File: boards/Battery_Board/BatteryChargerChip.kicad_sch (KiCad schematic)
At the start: 13 parts, among them J201 Conn_01x02, Q201 BSP613PH6327XTSA1, U201 BQ25185DLHR, U202 TCA6424

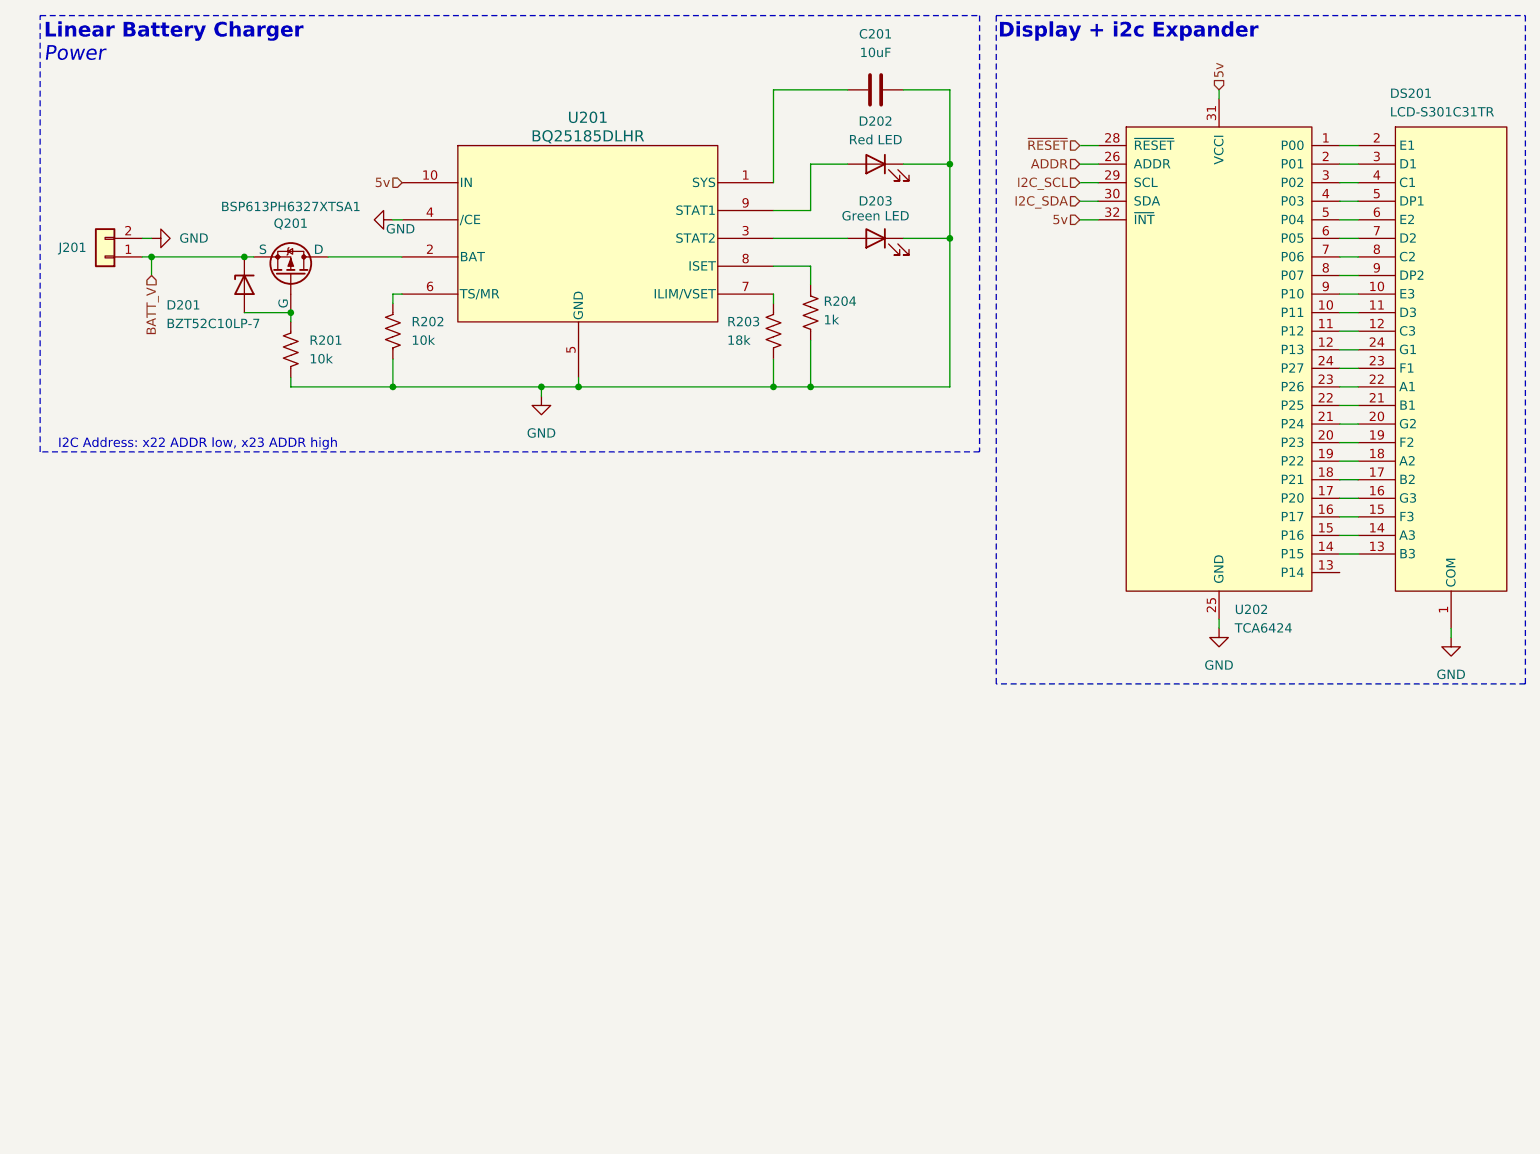
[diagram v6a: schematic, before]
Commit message: routing for displays 1-3
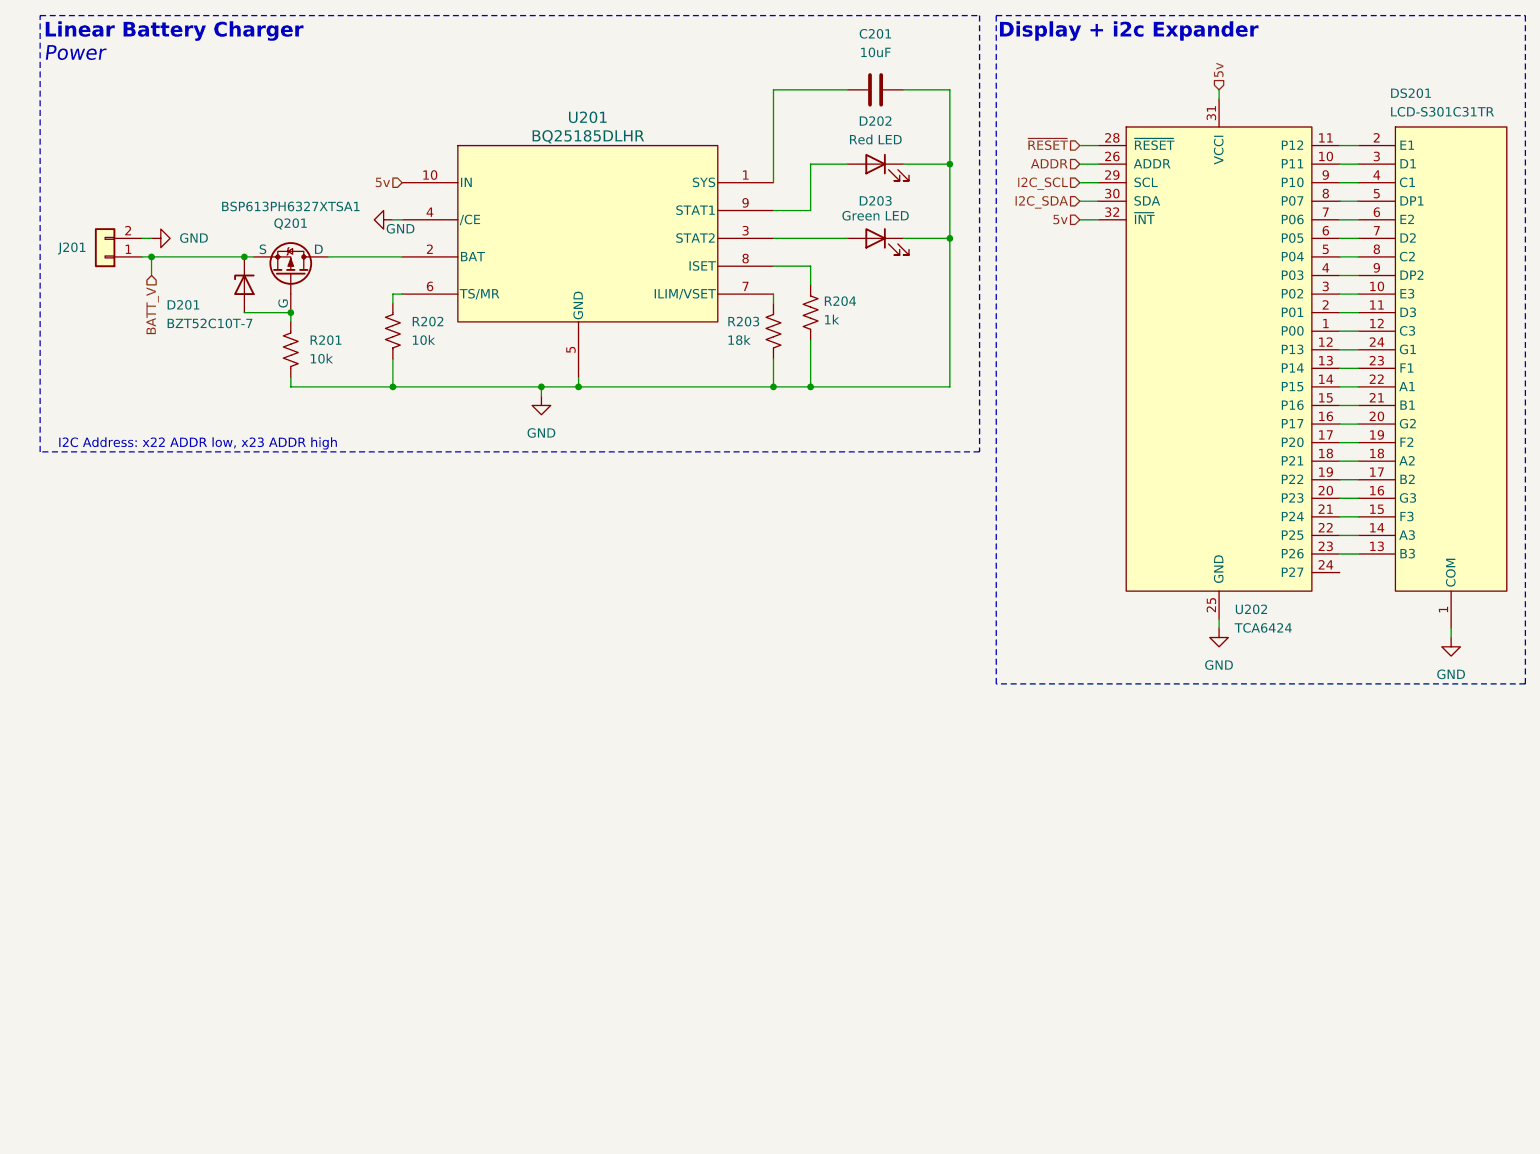
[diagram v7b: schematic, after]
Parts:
- D201: value BZT52C10LP-7 -> BZT52C10T-7; footprint Diode_SMD:D_0402_1005Metric -> Diode_SMD:D_SOD-523
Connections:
- net at DS201.10 (E3): now also U202.3 (P02); no longer U202.9 (P10)
- net at DS201.11 (D3): now also U202.2 (P01); no longer U202.10 (P11)
- net at DS201.12 (C3): now also U202.1 (P00); no longer U202.11 (P12)
- net at DS201.13 (B3): now also U202.23 (P26); no longer U202.14 (P15)
- net at DS201.14 (A3): now also U202.22 (P25); no longer U202.15 (P16)
- net at DS201.15 (F3): now also U202.21 (P24); no longer U202.16 (P17)
- net at DS201.16 (G3): now also U202.20 (P23); no longer U202.17 (P20)
- net at DS201.17 (B2): now also U202.19 (P22); no longer U202.18 (P21)
- net at DS201.18 (A2): now also U202.18 (P21); no longer U202.19 (P22)
- net at DS201.19 (F2): now also U202.17 (P20); no longer U202.20 (P23)
- net at DS201.2 (E1): now also U202.11 (P12); no longer U202.1 (P00)
- net at DS201.20 (G2): now also U202.16 (P17); no longer U202.21 (P24)
- net at DS201.21 (B1): now also U202.15 (P16); no longer U202.22 (P25)
- net at DS201.22 (A1): now also U202.14 (P15); no longer U202.23 (P26)
- net at DS201.23 (F1): now also U202.13 (P14); no longer U202.24 (P27)
- net at DS201.3 (D1): now also U202.10 (P11); no longer U202.2 (P01)
- net at DS201.4 (C1): now also U202.9 (P10); no longer U202.3 (P02)
- net at DS201.5 (DP1): now also U202.8 (P07); no longer U202.4 (P03)
- net at DS201.6 (E2): now also U202.7 (P06); no longer U202.5 (P04)
- net at DS201.8 (C2): now also U202.5 (P04); no longer U202.7 (P06)
- net at DS201.9 (DP2): now also U202.4 (P03); no longer U202.8 (P07)

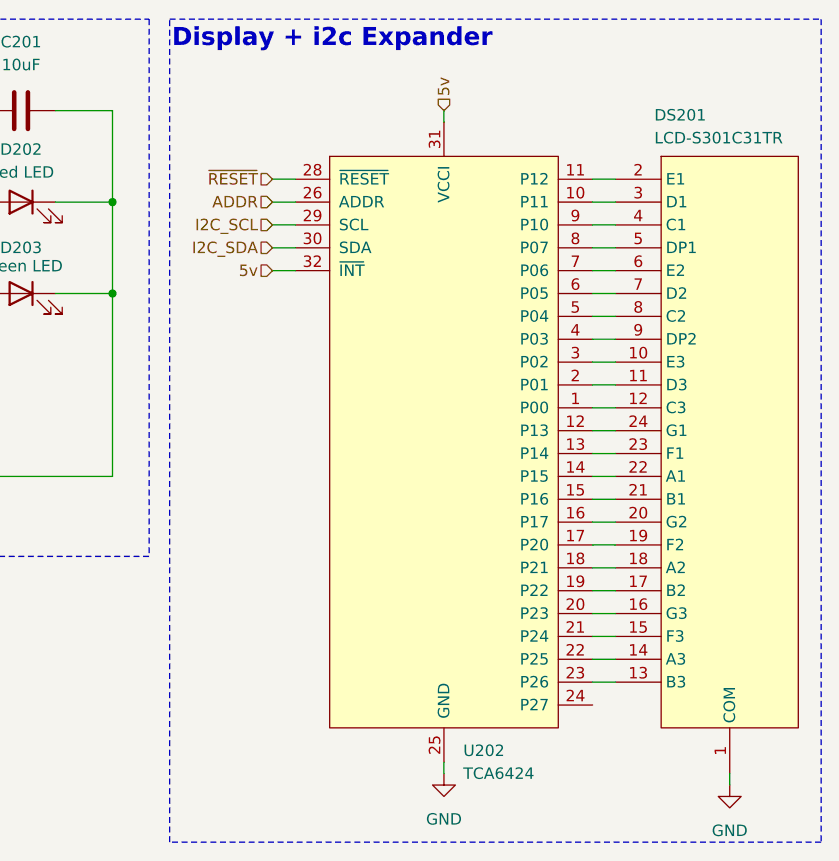
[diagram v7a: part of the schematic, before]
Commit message: Display Board
Added symbol for Display board, edited pull-up resistors and microcontroller expander to match the pins on the display board symbol.
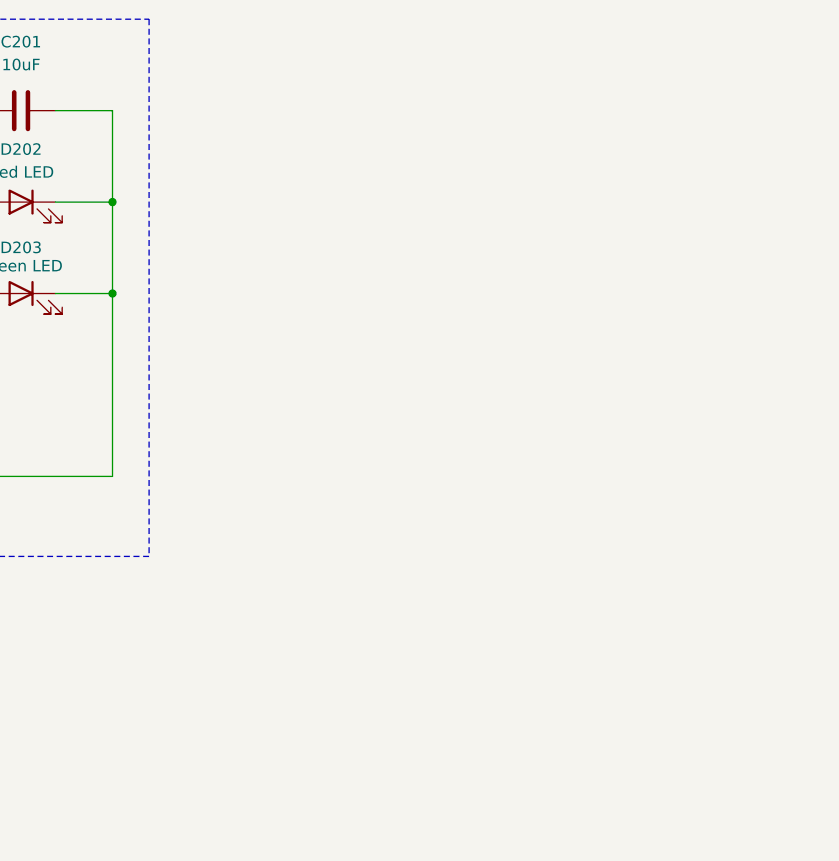
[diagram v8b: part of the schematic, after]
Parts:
- removed DS201: LCD-S301C31TR, Lumex:LCD-S301C31TR, symbol Lumex_Display:LCD-S301C31TR
- removed U202: TCA6424, Package_DFN_QFN:UQFN-32_5x5mm_P0.5mm, symbol Interface_Expander_Texas:TCA6424
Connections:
- net VCCP renamed 5v
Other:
- note removed: "Display + i2c Expander"
